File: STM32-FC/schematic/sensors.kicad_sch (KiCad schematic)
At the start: 18 parts, among them J5 JST ZH 1.5mm 2P, U6 BMI323, U7 ICM-42688-P, U8 LIS2MDLTR, U9 LPS22HH

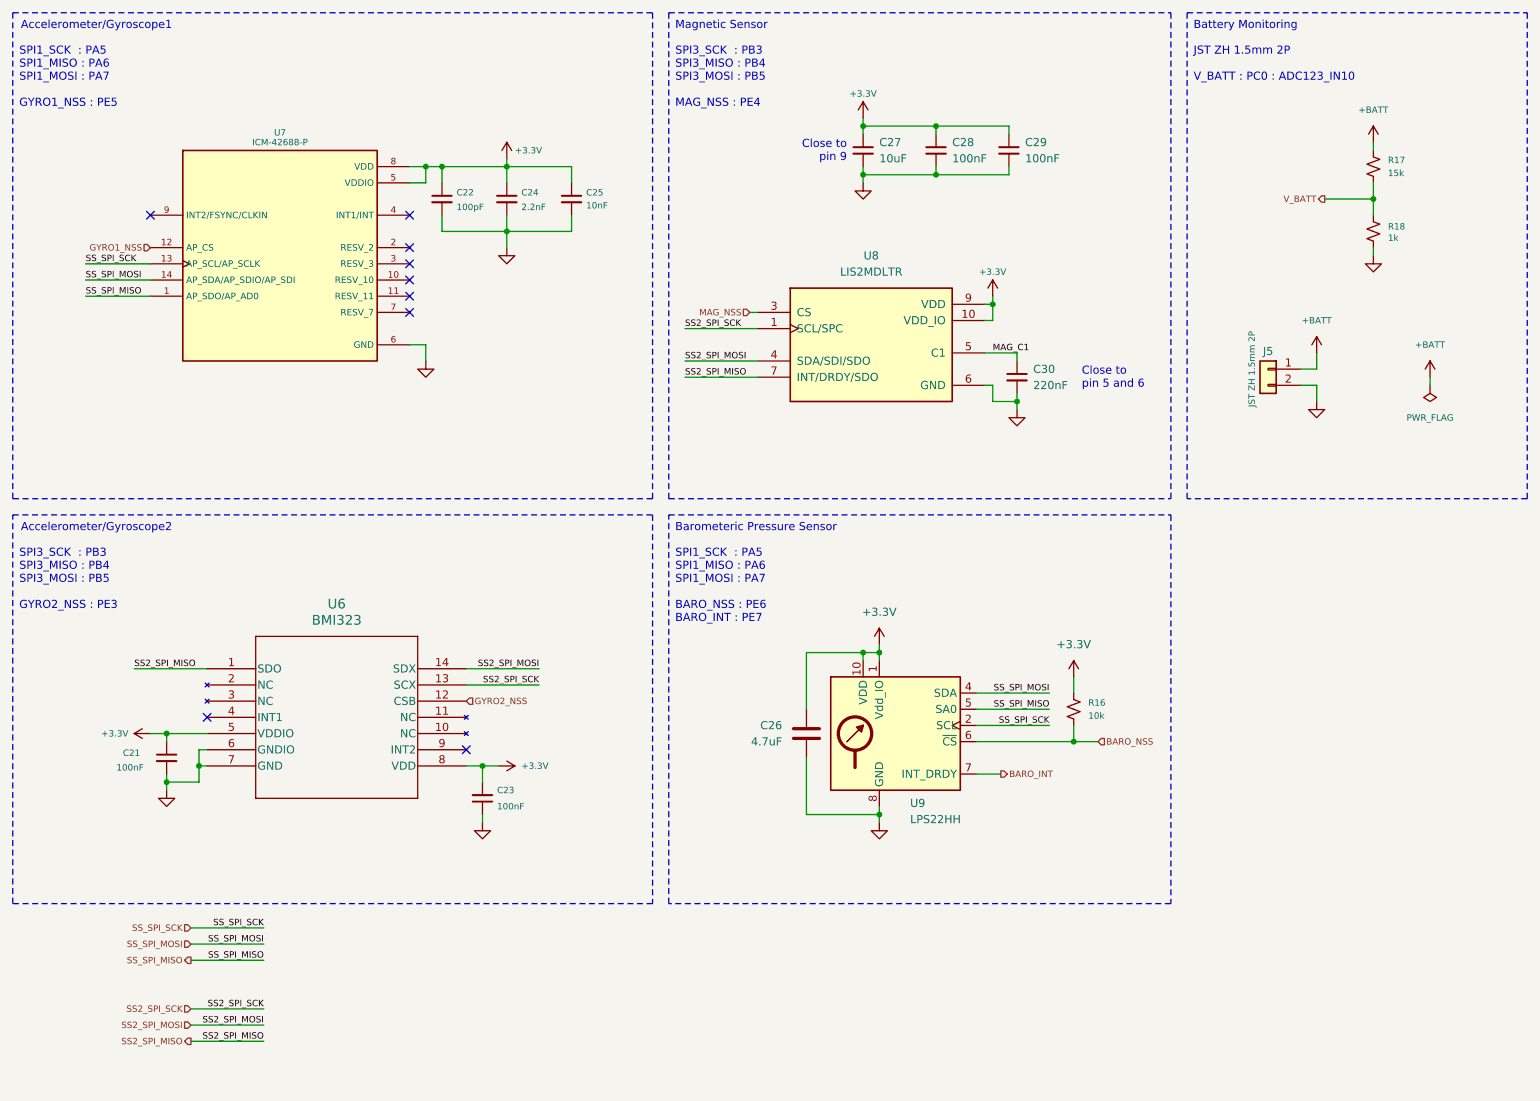
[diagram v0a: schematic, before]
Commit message: v1.0.1 update WIP
repactor and USB C bug fix
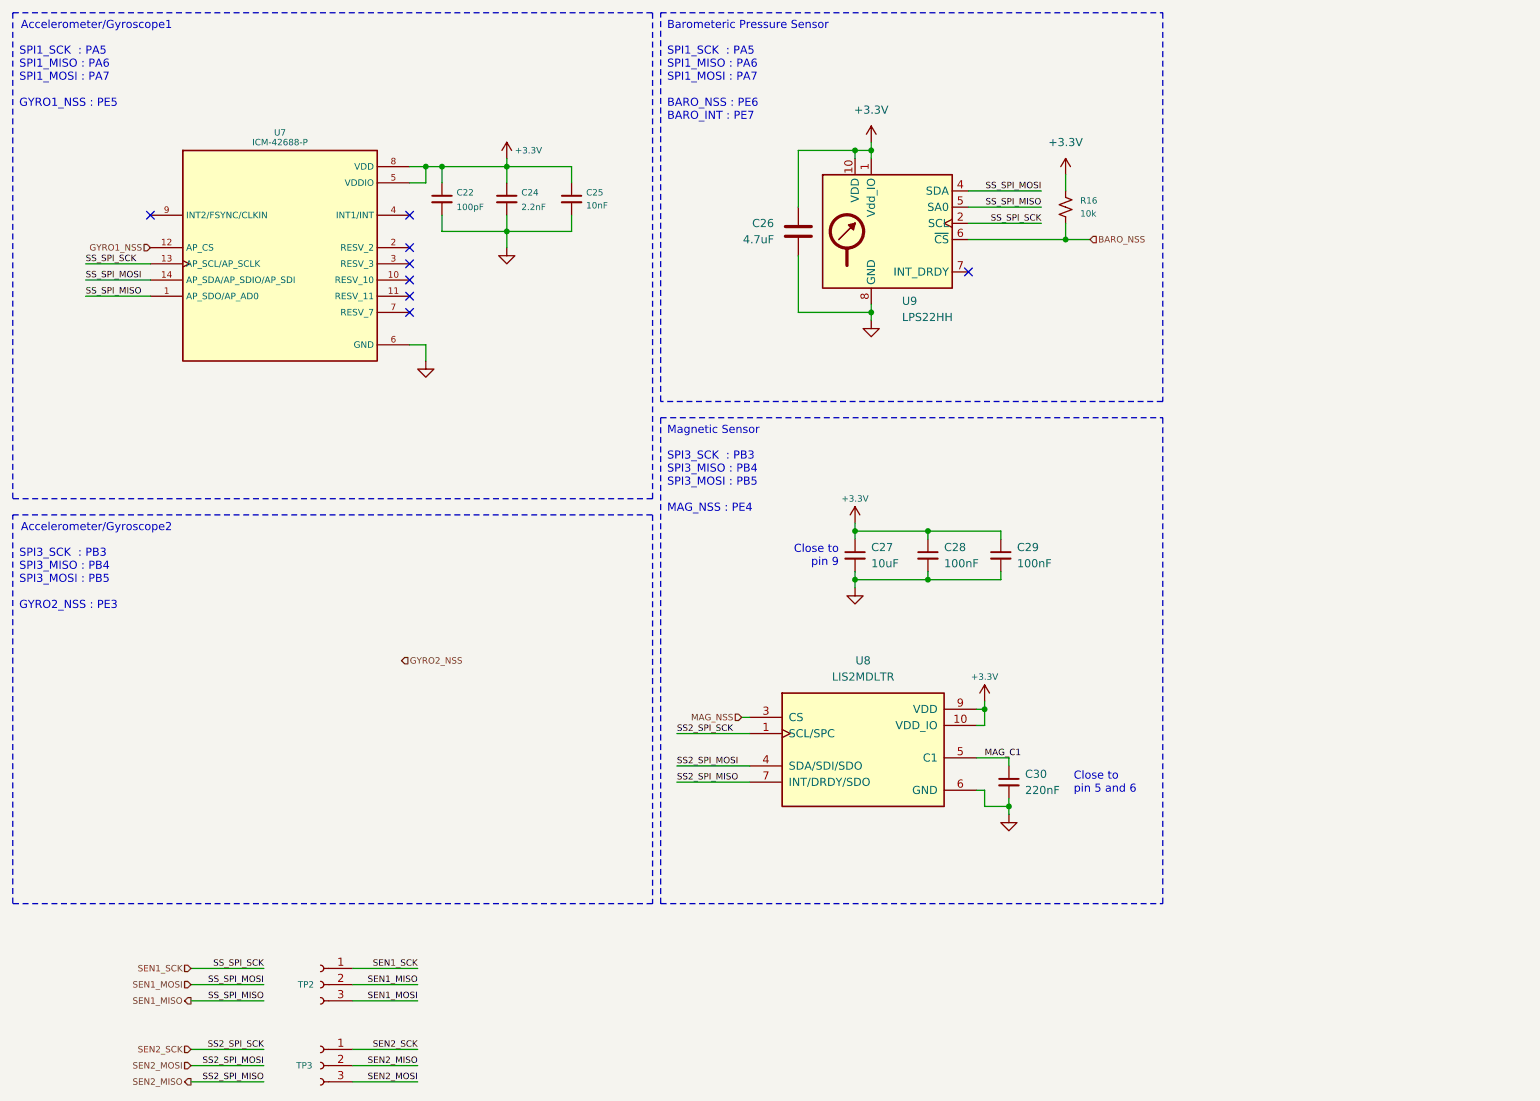
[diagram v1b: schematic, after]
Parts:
- removed C21, C23: 100nF, Capacitor_SMD:C_0402_1005Metric, symbol Device:C_Small
- removed J5: JST ZH 1.5mm 2P, JST_ZH:JST_ZH_S2B-ZR-SM4A-TF_1x02-1MP_P1.50mm_Horizontal, symbol Connector_Generic:Conn_01x02
- removed R17: 15k, Resistor_SMD:R_0402_1005Metric, symbol Device:R_Small_US
- removed R18: 1k, Resistor_SMD:R_0402_1005Metric, symbol Device:R_Small_US
- removed U6: BMI323, BMI323:BMI323_L, symbol BMI323:BMI323
- added TP2, TP3: Test Pin, Connector_PinHeader_1.27mm:PinHeader_1x03_P1.27mm_Vertical, symbol Connector:Conn_01x03_Socket
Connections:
- net BARO_INT: no longer names the net of U9.7 (INT_DRDY)
- net SS2_SPI_MISO renamed SEN2_MISO
- net SEN2_MISO: now also TP3.2 (Pin_2)
- net SS2_SPI_MOSI renamed SEN2_MOSI
- net SEN2_MOSI: now also TP3.3 (Pin_3)
- net SS2_SPI_SCK renamed SEN2_SCK
- net SEN2_SCK: now also TP3.1 (Pin_1)
- net SS_SPI_MISO renamed SEN1_MISO
- net SEN1_MISO: now also TP2.2 (Pin_2)
- net SS_SPI_MOSI renamed SEN1_MOSI
- net SEN1_MOSI: now also TP2.3 (Pin_3)
- net SS_SPI_SCK renamed SEN1_SCK
- net SEN1_SCK: now also TP2.1 (Pin_1)
- no-connect marks 9 -> 8
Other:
- note removed: "Battery Monitoring"
- note removed: "JST ZH 1.5mm 2P V_BATT : PC0 : ADC123_IN10"
- moved on the sheet: C26, C27, C28, C29, C30, R16, U8, U9

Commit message: schematic update & lib update
- ICM-45686
- ICP-20100
- Micro SD update SDIO instead of SPI
- servo main output
- DC2DC buck instead power regulator
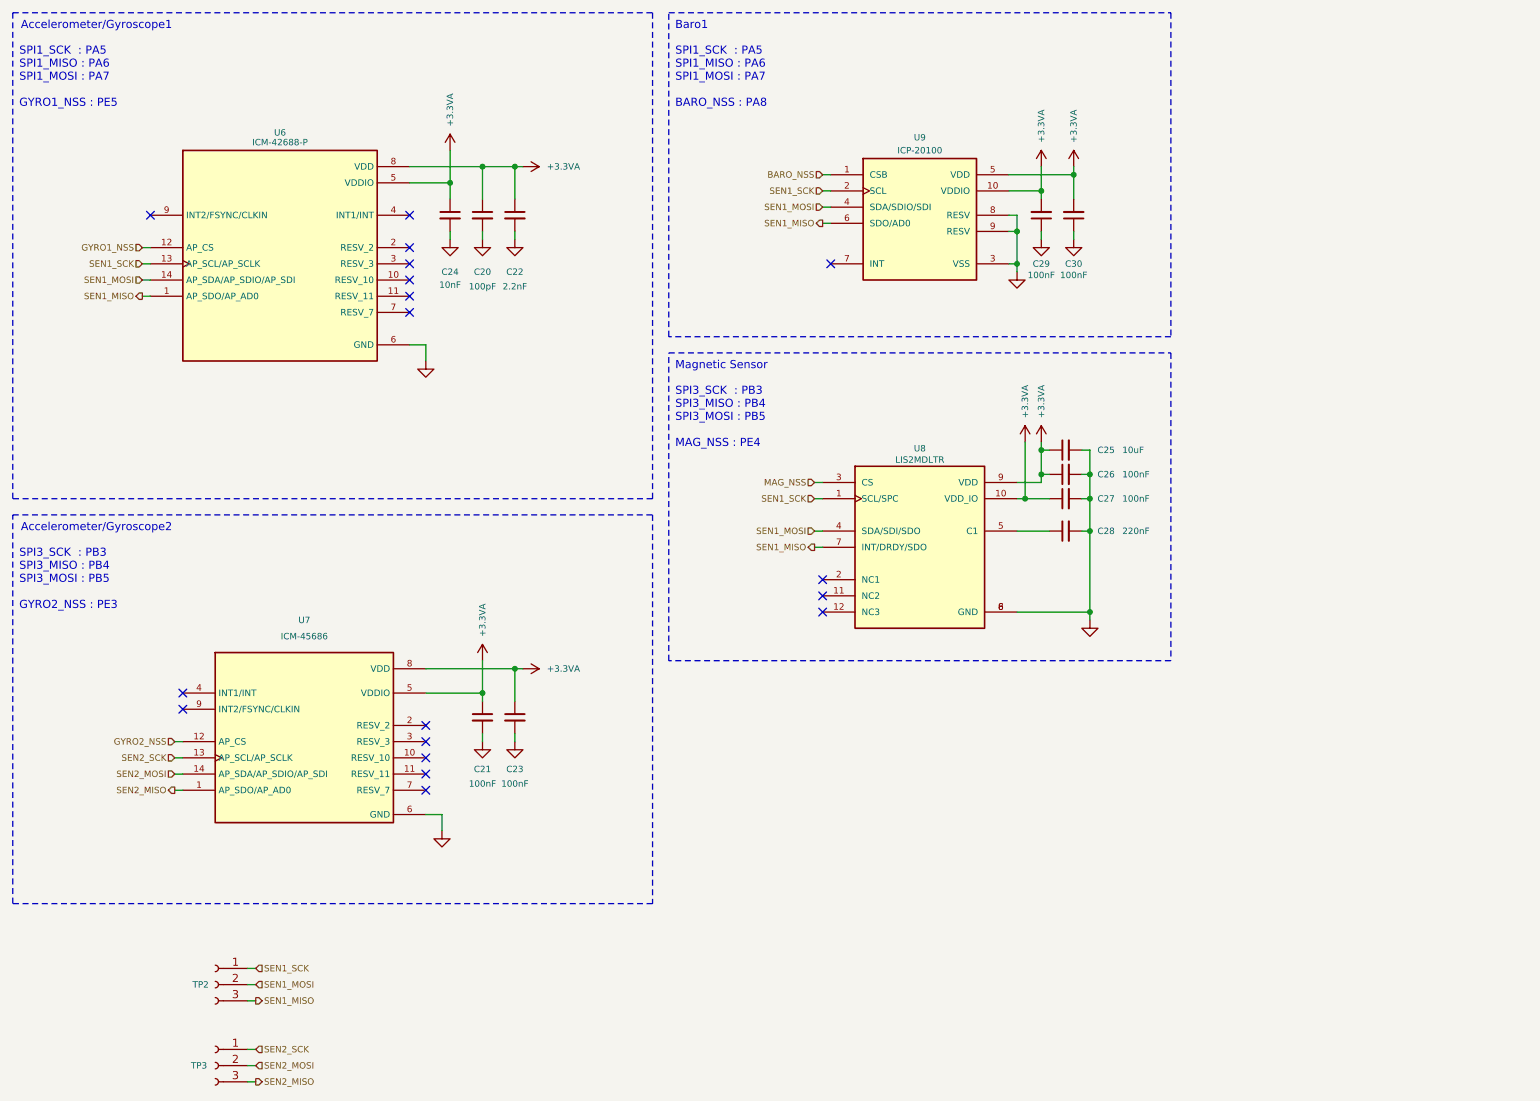
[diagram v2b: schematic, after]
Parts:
- removed C26: 4.7uF, Capacitor_SMD:C_0402_1005Metric, symbol Device:C
- removed R16: 10k, Resistor_SMD:R_0402_1005Metric, symbol Device:R_Small_US
- removed U9: LPS22HH, LPS22HH:ST_HLGA-10_2x2mm_P0.5mm_LayoutBorder3x2y, symbol Sensor_Pressure:LPS22HH
- added C20: 100pF, Capacitor_SMD:C_0402_1005Metric, symbol Device:C_Small
- added C21, C29, C30: 100nF, Capacitor_SMD:C_0402_1005Metric, symbol Device:C_Small
- added U7: ICM-45686, ICM-45686:ICM-45686, symbol ICM-45686:ICM-45686
- added U9: ICP-20100, ICP-20100:ICP-20100, symbol ICP-20100:ICP-20100
- C23: renamed from C22; value 100pF -> 100nF; LCSC C152819 -> C1525
- C25: renamed from C27; LCSC C77000 -> C307415
- renumbered C24 to C22, C25 to C24, C28 to C26, C29 to C27, C30 to C28, U7 to U6
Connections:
- net BARO_NSS: now also U9.1 (CSB)
- net GND: now also C20.2, C21.2, C29.1, C30.1, U7.6 (GND), U9.3 (VSS), U9.8 (RESV), U9.9 (RESV)
- net GYRO2_NSS: now also U7.12 (AP_CS)
- net SEN1_MISO: now also TP2.3 (Pin_3), U8.7 (INT/DRDY/SDO), U9.6 (SDO/AD0); no longer TP2.2 (Pin_2)
- net SEN1_MOSI: now also TP2.2 (Pin_2), U8.4 (SDA/SDI/SDO), U9.4 (SDA/SDIO/SDI); no longer TP2.3 (Pin_3)
- net SEN1_SCK: now also U8.1 (SCL/SPC), U9.2 (SCL)
- net SEN2_MISO: now also TP3.3 (Pin_3), U7.1 (AP_SDO/AP_AD0); no longer TP3.2 (Pin_2), U8.7 (INT/DRDY/SDO)
- net SEN2_MOSI: now also TP3.2 (Pin_2), U7.14 (AP_SDA/AP_SDIO/AP_SDI); no longer TP3.3 (Pin_3), U8.4 (SDA/SDI/SDO)
- net SEN2_SCK: now also U7.13 (AP_SCL/AP_SCLK); no longer U8.1 (SCL/SPC)
- net +3.3V renamed +3.3VA
- net +3.3VA: now also C20.1, C21.1, C29.2, C30.2, U7.5 (VDDIO), U7.8 (VDD), U9.10 (VDDIO), U9.5 (VDD)
- net MAG_C1: no longer names the net of C28.1, U8.5 (C1)
- no-connect marks 8 -> 18
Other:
- note added: "Baro1"
- note added: "SPI1_SCK : PA5 SPI1_MISO : PA6 SPI1_MOSI : PA7 BARO_NSS : PA8"
- note removed: "Barometeric Pressure Sensor"
- note removed: "Close to pin 5 and 6"
- note removed: "Close to pin 9"
- note removed: "SPI1_SCK : PA5 SPI1_MISO : PA6 SPI1_MOSI : PA7 BARO_NSS : PE6 BARO_INT : PE7"
- title: STM32 Flight Controller -> NARAEON - Flight Controller
- moved on the sheet: C22, C23, C24, C25, C26, C27, C28, TP2, TP3

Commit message: add: servo power & comment
- Servo power diode add
- comment update
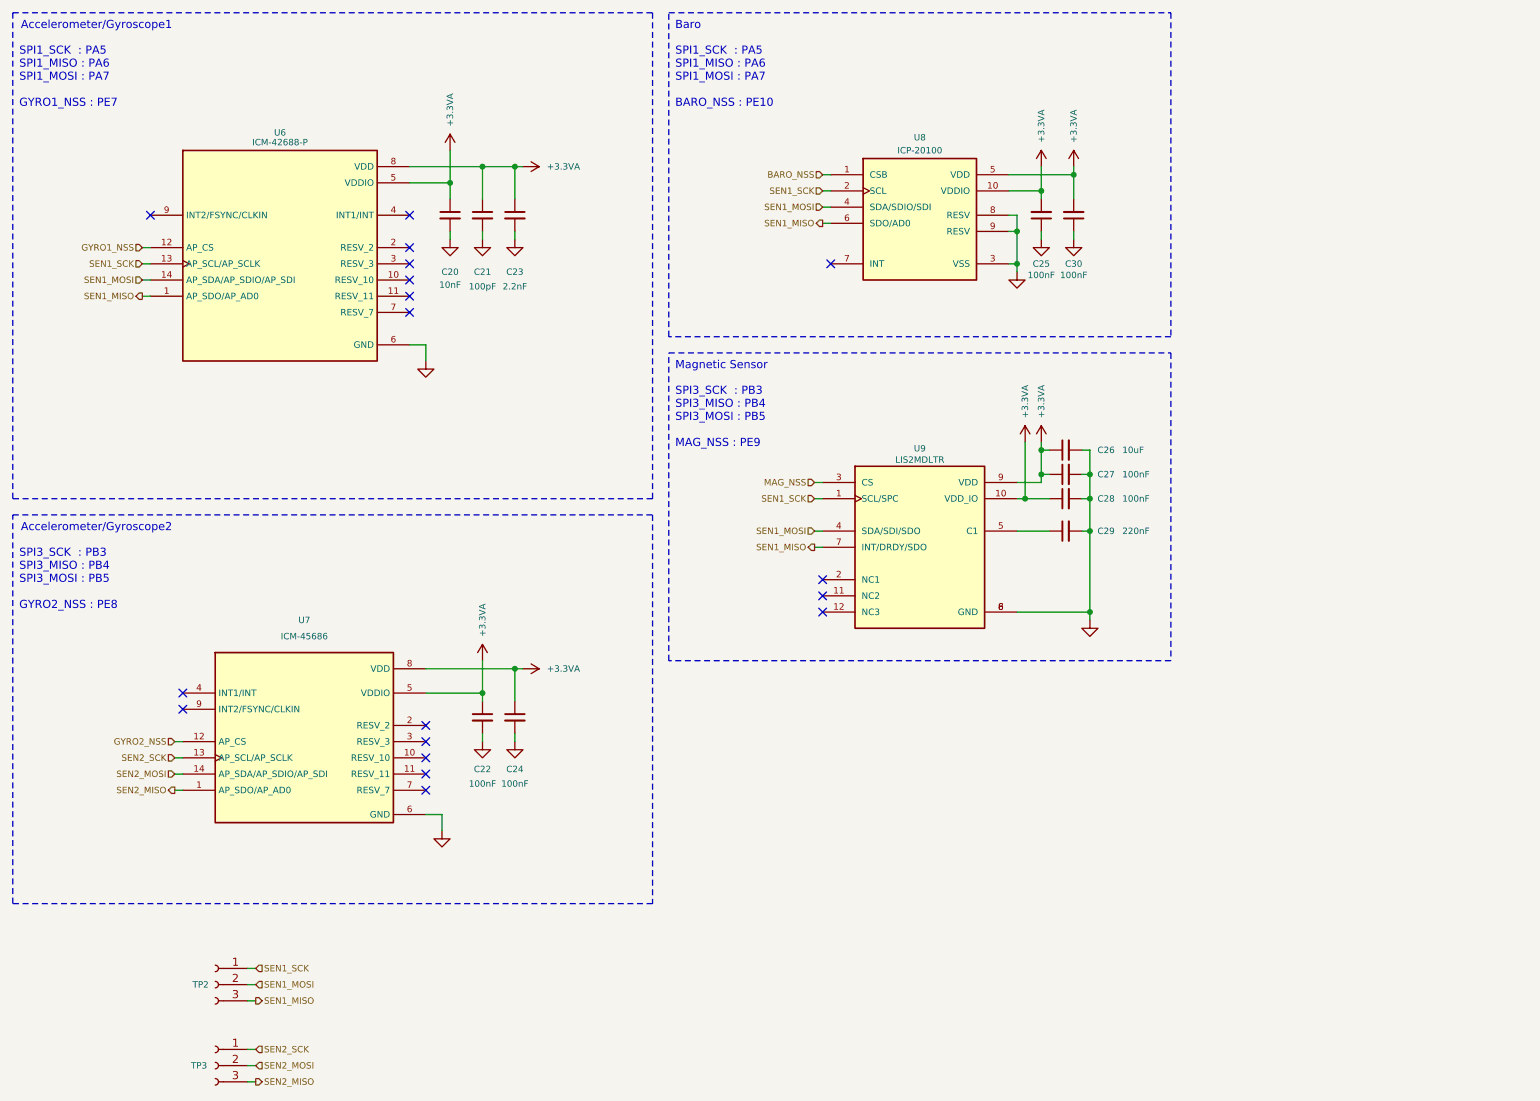
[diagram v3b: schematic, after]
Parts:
- renumbered C24 to C20, C20 to C21, C21 to C22, C22 to C23, C23 to C24, C29 to C25, C25 to C26, C26 to C27, C27 to C28, C28 to C29, U9 to U8, U8 to U9
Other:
- note added: "Baro"
- note added: "SPI1_SCK : PA5 SPI1_MISO : PA6 SPI1_MOSI : PA7 BARO_NSS : PE10"
- note added: "SPI1_SCK : PA5 SPI1_MISO : PA6 SPI1_MOSI : PA7 GYRO1_NSS : PE7"
- note added: "SPI3_SCK : PB3 SPI3_MISO : PB4 SPI3_MOSI : PB5 GYRO2_NSS : PE8"
- note added: "SPI3_SCK : PB3 SPI3_MISO : PB4 SPI3_MOSI : PB5 MAG_NSS : PE9"
- note removed: "Baro1"
- note removed: "SPI1_SCK : PA5 SPI1_MISO : PA6 SPI1_MOSI : PA7 BARO_NSS : PA8"
- note removed: "SPI1_SCK : PA5 SPI1_MISO : PA6 SPI1_MOSI : PA7 GYRO1_NSS : PE5"
- note removed: "SPI3_SCK : PB3 SPI3_MISO : PB4 SPI3_MOSI : PB5 GYRO2_NSS : PE3"
- note removed: "SPI3_SCK : PB3 SPI3_MISO : PB4 SPI3_MOSI : PB5 MAG_NSS : PE4"

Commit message: WIP : pcb part layout &* BOM udpate
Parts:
- U8: Availability In Stock -> (none); Check_prices https://www.snapeda.com/parts/ICP-20100/TDK/view-part/?ref=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 -> (none); Description_1 Pressure Sensor 4.35PSI ~ 15.95PSI (30kPa ~ 110kPa) Absolut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 -> (none); MANUFACTURER TDK InvenSense -> (none); MAXIMUM_PACKAGE_HEIGHT 0.85mm -> (none); MF TDK InvenSense -> (none); MP ICP-20100 -> (none); PARTREV 1.1 -> (none); Package None -> (none); Price None -> (none); STANDARD IPC 7351B -> (none); SnapEDA_Link https://www.snapeda.com/parts/ICP-20100/TDK/view-part/?ref=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 -> (none)
- U9: value LIS2MDLTR -> LIS2MDLRT

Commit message: update : AHRS PCB layout & routing done
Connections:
- net SEN1_MISO: no longer U9.7 (INT/DRDY/SDO)
- net SEN1_MOSI: no longer U9.4 (SDA/SDI/SDO)
- net SEN1_SCK: no longer U9.1 (SCL/SPC)
- net SEN2_MISO: now also U9.7 (INT/DRDY/SDO)
- net SEN2_MOSI: now also U9.4 (SDA/SDI/SDO)
- net SEN2_SCK: now also U9.1 (SCL/SPC)
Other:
- note added: "SPI2_SCK : PB13 SPI2_MISO : PB14 SPI2_MOSI : PB15 GYRO2_NSS : PE8"
- note added: "SPI2_SCK : PB13 SPI2_MISO : PB14 SPI2_MOSI : PB15 MAG_NSS : PE9"
- note removed: "SPI3_SCK : PB3 SPI3_MISO : PB4 SPI3_MOSI : PB5 GYRO2_NSS : PE8"
- note removed: "SPI3_SCK : PB3 SPI3_MISO : PB4 SPI3_MOSI : PB5 MAG_NSS : PE9"

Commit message: PCB layout done
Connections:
- net GND renamed GNDA
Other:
- note added: "SPI1_SCK : PA5 SPI1_MISO : PA6 SPI1_MOSI : PA7 GYRO1_NSS : PB1"
- note removed: "SPI1_SCK : PA5 SPI1_MISO : PA6 SPI1_MOSI : PA7 GYRO1_NSS : PE7"
